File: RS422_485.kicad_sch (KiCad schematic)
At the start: 10 parts, among them U8501 THVD1424

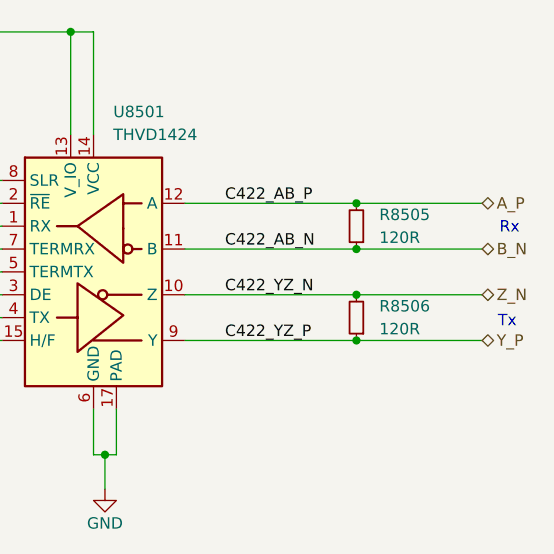
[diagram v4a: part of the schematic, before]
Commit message: added missing heater connectors
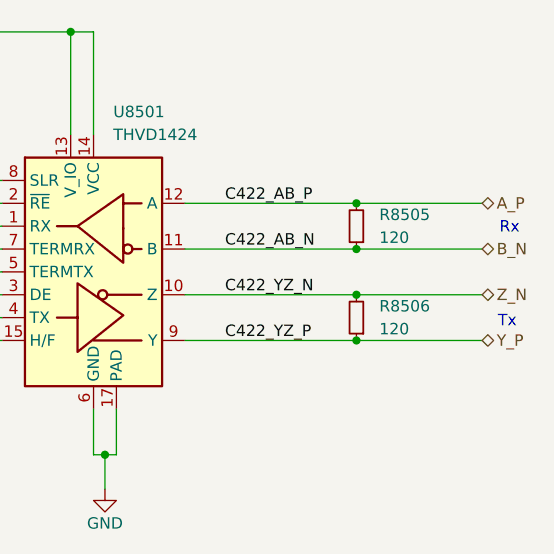
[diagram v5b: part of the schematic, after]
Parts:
- R8505, R8506: value 120R -> 120
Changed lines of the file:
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@@
 			)
 		)
-		(property "Value" "120R"
+		(property "Value" "120"
 			(at 219.71 100.3299 0)
 			(effects
@@
 			)
 		)
-		(property "Value" "120R"
+		(property "Value" "120"
 			(at 219.71 110.4899 0)
 			(effects

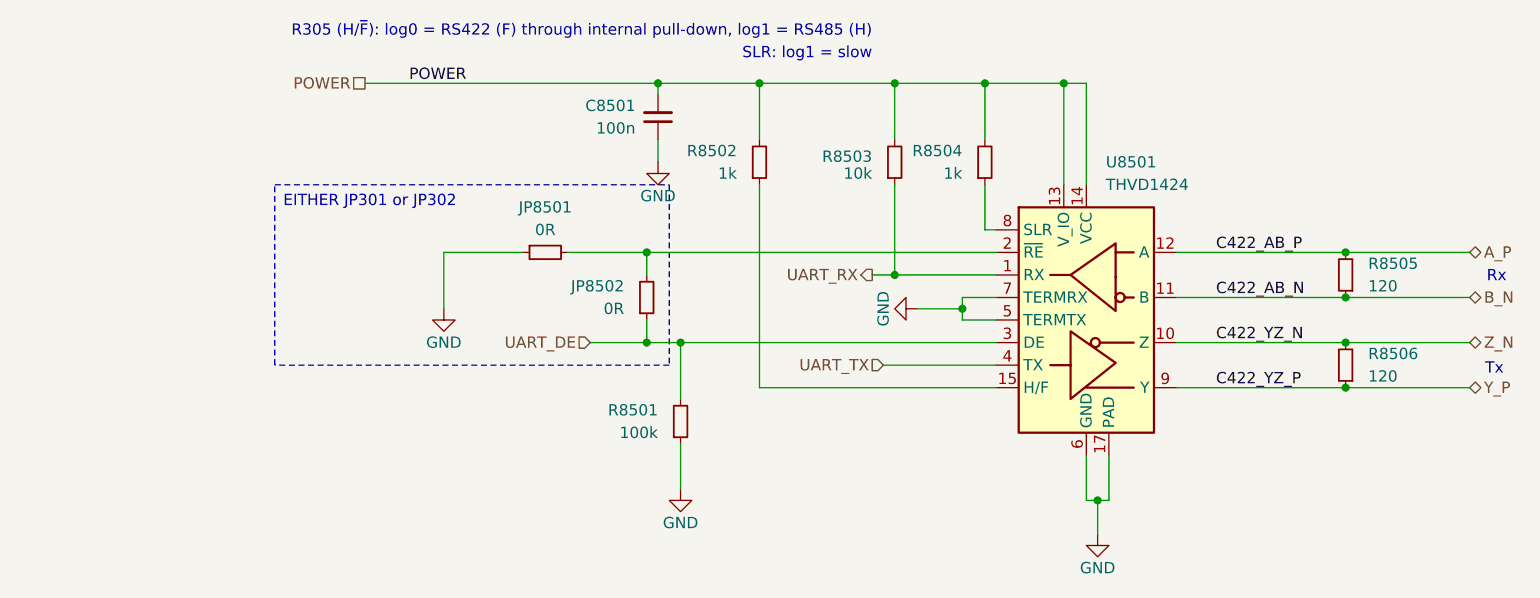
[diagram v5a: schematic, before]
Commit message: restructurization of the entire project improved
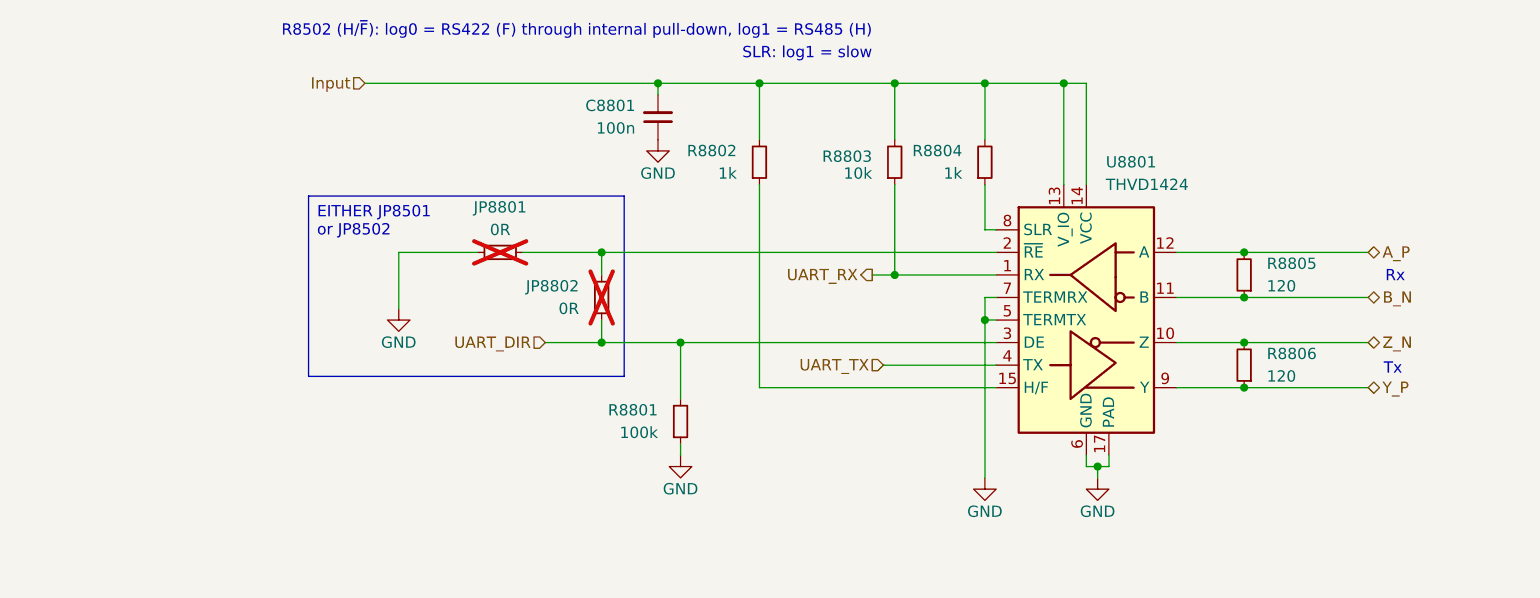
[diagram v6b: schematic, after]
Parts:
- JP8801: renamed from JP8501; now not fitted
- JP8802: renamed from JP8502; now not fitted
- renumbered C8501 to C8801, R8501 to R8801, R8502 to R8802, R8503 to R8803, R8504 to R8804, R8505 to R8805, R8506 to R8806, U8501 to U8801
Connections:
- net POWER renamed Input
- net UART_DE renamed UART_DIR
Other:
- note added: "R8502 (H/~{F}): log0 = RS422 (F) through internal pull-down, log1 = RS485 (H)"
- note removed: "R305 (H/~{F}): log0 = RS422 (F) through internal pull-down, log1 = RS485 (H)"
- moved on the sheet: R8805, R8806

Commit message: added universal switch, added simples current source, reworked test schematic and pcb
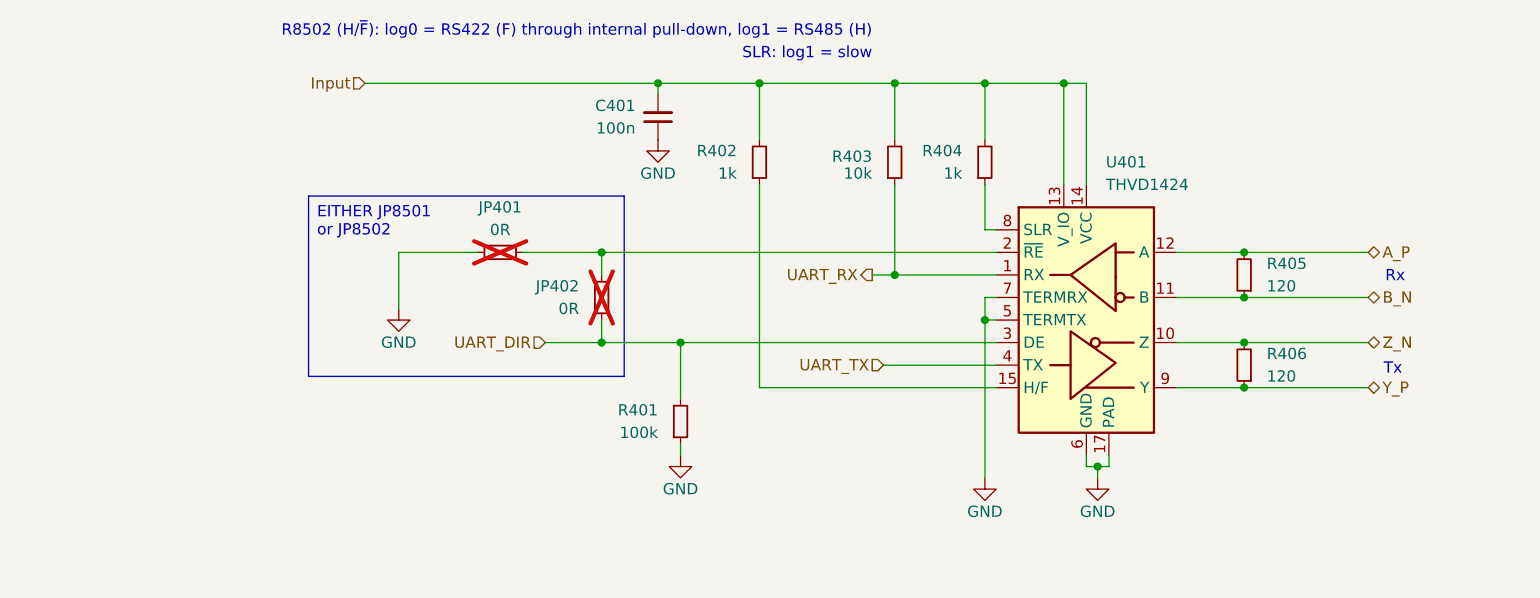
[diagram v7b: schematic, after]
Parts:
- C401: renamed from C8801; footprint Capacitor_SMD:C_0603_1608Metric -> Capacitor_SMD:C_0603_1608Metric_Pad1.08x0.95mm_HandSolder
- renumbered JP8801 to JP401, JP8802 to JP402, R8801 to R401, R8802 to R402, R8803 to R403, R8804 to R404, R8805 to R405, R8806 to R406, U8801 to U401
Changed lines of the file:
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@@
 		(on_board yes)
 		(dnp no)
-		(property "Reference" "R8805"
+		(property "Reference" "R405"
 			(at 208.28 97.7899 0)
 			(effects
@@
 		)
 		(instances
+			(project "EPS_CORE"
+				(path "/29496ace-b476-4f24-a65f-9da1dd70122c/59fca87d-eab6-4325-93c7-8130e49f891e/6fcf384b-60b0-45a5-8dc1-cf23d8e5c23c"
+					(reference "R405")
+					(unit 1)
+				)
+			)
 			(project "EPS_CORE"
 				(path "/43e5e7c8-e7e0-4528-9a3e-b1557849918d/ce55ed75-3d20-4bd3-84d2-d62dbd0d02de/6fcf384b-60b0-45a5-8dc1-cf23d8e5c23c"
@@
 		(on_board yes)
 		(dnp no)
-		(property "Reference" "R8803"
+		(property "Reference" "R403"
 			(at 163.83 85.725 0)
 			(effects
@@
 		)
 		(instances
+			(project "EPS_CORE"
+				(path "/29496ace-b476-4f24-a65f-9da1dd70122c/59fca87d-eab6-4325-93c7-8130e49f891e/6fcf384b-60b0-45a5-8dc1-cf23d8e5c23c"
+					(reference "R403")
+					(unit 1)
+				)
+			)
 			(project "EPS_CORE"
 				(path "/43e5e7c8-e7e0-4528-9a3e-b1557849918d/ce55ed75-3d20-4bd3-84d2-d62dbd0d02de/6fcf384b-60b0-45a5-8dc1-cf23d8e5c23c"
@@
 		(dnp yes)
 		(fields_autoplaced yes)
-		(property "Reference" "JP8801"
+		(property "Reference" "JP401"
 			(at 121.92 91.44 90)
 			(effects
@@
 		)
 		(instances
+			(project "EPS_CORE"
+				(path "/29496ace-b476-4f24-a65f-9da1dd70122c/59fca87d-eab6-4325-93c7-8130e49f891e/6fcf384b-60b0-45a5-8dc1-cf23d8e5c23c"
+					(reference "JP401")
+					(unit 1)
+				)
+			)
 			(project "EPS_CORE"
 				(path "/43e5e7c8-e7e0-4528-9a3e-b1557849918d/ce55ed75-3d20-4bd3-84d2-d62dbd0d02de/6fcf384b-60b0-45a5-8dc1-cf23d8e5c23c"
@@
 		(on_board yes)
 		(dnp no)
-		(property "Reference" "#PWR08803"
+		(property "Reference" "#PWR0403"
 			(at 142.24 125.73 0)
 			(effects
@@
 		)
 		(instances
+			(project "EPS_CORE"
+				(path "/29496ace-b476-4f24-a65f-9da1dd70122c/59fca87d-eab6-4325-93c7-8130e49f891e/6fcf384b-60b0-45a5-8dc1-cf23d8e5c23c"
+					(reference "#PWR0403")
+					(unit 1)
+				)
+			)
 			(project "EPS_CORE"
 				(path "/43e5e7c8-e7e0-4528-9a3e-b1557849918d/ce55ed75-3d20-4bd3-84d2-d62dbd0d02de/6fcf384b-60b0-45a5-8dc1-cf23d8e5c23c"
@@
 		(dnp no)
 		(fields_autoplaced yes)
-		(property "Reference" "C8801"
+		(property "Reference" "C401"
 			(at 137.16 80.0035 0)
 			(effects
@@
 			)
 		)
-		(property "Footprint" "Capacitor_SMD:C_0603_1608Metric"
+		(property "Footprint" "Capacitor_SMD:C_0603_1608Metric_Pad1.08x0.95mm_HandSolder"
 			(at 139.7 81.28 0)
 			(effects
@@
 		)
 		(instances
+			(project "EPS_CORE"
+				(path "/29496ace-b476-4f24-a65f-9da1dd70122c/59fca87d-eab6-4325-93c7-8130e49f891e/6fcf384b-60b0-45a5-8dc1-cf23d8e5c23c"
+					(reference "C401")
+					(unit 1)
+				)
+			)
 			(project "EPS_CORE"
 				(path "/43e5e7c8-e7e0-4528-9a3e-b1557849918d/ce55ed75-3d20-4bd3-84d2-d62dbd0d02de/6fcf384b-60b0-45a5-8dc1-cf23d8e5c23c"
@@
 		(dnp no)
 		(fields_autoplaced yes)
-		(property "Reference" "R8802"
+		(property "Reference" "R402"
 			(at 148.59 85.09 0)
 			(effects
@@
 		)
 		(instances
+			(project "EPS_CORE"
+				(path "/29496ace-b476-4f24-a65f-9da1dd70122c/59fca87d-eab6-4325-93c7-8130e49f891e/6fcf384b-60b0-45a5-8dc1-cf23d8e5c23c"
+					(reference "R402")
+					(unit 1)
+				)
+			)
 			(project "EPS_CORE"
 				(path "/43e5e7c8-e7e0-4528-9a3e-b1557849918d/ce55ed75-3d20-4bd3-84d2-d62dbd0d02de/6fcf384b-60b0-45a5-8dc1-cf23d8e5c23c"
@@
 		(on_board yes)
 		(dnp no)
-		(property "Reference" "#PWR08805"
+		(property "Reference" "#PWR0405"
 			(at 189.23 128.27 0)
 			(effects
@@
 		)
 		(instances
+			(project "EPS_CORE"
+				(path "/29496ace-b476-4f24-a65f-9da1dd70122c/59fca87d-eab6-4325-93c7-8130e49f891e/6fcf384b-60b0-45a5-8dc1-cf23d8e5c23c"
+					(reference "#PWR0405")
+					(unit 1)
+				)
+			)
 			(project "EPS_CORE"
 				(path "/43e5e7c8-e7e0-4528-9a3e-b1557849918d/ce55ed75-3d20-4bd3-84d2-d62dbd0d02de/6fcf384b-60b0-45a5-8dc1-cf23d8e5c23c"
@@
 		(dnp no)
 		(fields_autoplaced yes)
-		(property "Reference" "R8804"
+		(property "Reference" "R404"
 			(at 173.99 85.09 0)
 			(effects
@@
 		)
 		(instances
+			(project "EPS_CORE"
+				(path "/29496ace-b476-4f24-a65f-9da1dd70122c/59fca87d-eab6-4325-93c7-8130e49f891e/6fcf384b-60b0-45a5-8dc1-cf23d8e5c23c"
+					(reference "R404")
+					(unit 1)
+				)
+			)
 			(project "EPS_CORE"
 				(path "/43e5e7c8-e7e0-4528-9a3e-b1557849918d/ce55ed75-3d20-4bd3-84d2-d62dbd0d02de/6fcf384b-60b0-45a5-8dc1-cf23d8e5c23c"
@@
 		(on_board yes)
 		(dnp no)
-		(property "Reference" "#PWR08801"
+		(property "Reference" "#PWR0401"
 			(at 110.49 109.22 0)
 			(effects
@@
 		)
 		(instances
+			(project "EPS_CORE"
+				(path "/29496ace-b476-4f24-a65f-9da1dd70122c/59fca87d-eab6-4325-93c7-8130e49f891e/6fcf384b-60b0-45a5-8dc1-cf23d8e5c23c"
+					(reference "#PWR0401")
+					(unit 1)
+				)
+			)
 			(project "EPS_CORE"
 				(path "/43e5e7c8-e7e0-4528-9a3e-b1557849918d/ce55ed75-3d20-4bd3-84d2-d62dbd0d02de/6fcf384b-60b0-45a5-8dc1-cf23d8e5c23c"
@@
 		(dnp no)
 		(fields_autoplaced yes)
-		(property "Reference" "R8801"
+		(property "Reference" "R401"
 			(at 139.7 114.2999 0)
 			(effects
@@
 		)
 		(instances
+			(project "EPS_CORE"
+				(path "/29496ace-b476-4f24-a65f-9da1dd70122c/59fca87d-eab6-4325-93c7-8130e49f891e/6fcf384b-60b0-45a5-8dc1-cf23d8e5c23c"
+					(reference "R401")
+					(unit 1)
+				)
+			)
 			(project "EPS_CORE"
 				(path "/43e5e7c8-e7e0-4528-9a3e-b1557849918d/ce55ed75-3d20-4bd3-84d2-d62dbd0d02de/6fcf384b-60b0-45a5-8dc1-cf23d8e5c23c"
@@
 		(dnp no)
 		(fields_autoplaced yes)
-		(property "Reference" "U8801"
+		(property "Reference" "U401"
 			(at 190.1541 86.36 0)
 			(effects
@@
 		)
 		(instances
+			(project "EPS_CORE"
+				(path "/29496ace-b476-4f24-a65f-9da1dd70122c/59fca87d-eab6-4325-93c7-8130e49f891e/6fcf384b-60b0-45a5-8dc1-cf23d8e5c23c"
+					(reference "U401")
+					(unit 1)
+				)
+			)
 			(project "EPS_CORE"
 				(path "/43e5e7c8-e7e0-4528-9a3e-b1557849918d/ce55ed75-3d20-4bd3-84d2-d62dbd0d02de/6fcf384b-60b0-45a5-8dc1-cf23d8e5c23c"
@@
 		(on_board yes)
 		(dnp no)
-		(property "Reference" "#PWR08804"
+		(property "Reference" "#PWR0404"
 			(at 176.53 128.27 0)
 			(effects
@@
 		)
 		(instances
+			(project "EPS_CORE"
+				(path "/29496ace-b476-4f24-a65f-9da1dd70122c/59fca87d-eab6-4325-93c7-8130e49f891e/6fcf384b-60b0-45a5-8dc1-cf23d8e5c23c"
+					(reference "#PWR0404")
+					(unit 1)
+				)
+			)
 			(project "EPS_CORE"
 				(path "/43e5e7c8-e7e0-4528-9a3e-b1557849918d/ce55ed75-3d20-4bd3-84d2-d62dbd0d02de/6fcf384b-60b0-45a5-8dc1-cf23d8e5c23c"
@@
 		(on_board yes)
 		(dnp no)
-		(property "Reference" "R8806"
+		(property "Reference" "R406"
 			(at 208.28 107.9499 0)
 			(effects
@@
 		)
 		(instances
+			(project "EPS_CORE"
+				(path "/29496ace-b476-4f24-a65f-9da1dd70122c/59fca87d-eab6-4325-93c7-8130e49f891e/6fcf384b-60b0-45a5-8dc1-cf23d8e5c23c"
+					(reference "R406")
+					(unit 1)
+				)
+			)
 			(project "EPS_CORE"
 				(path "/43e5e7c8-e7e0-4528-9a3e-b1557849918d/ce55ed75-3d20-4bd3-84d2-d62dbd0d02de/6fcf384b-60b0-45a5-8dc1-cf23d8e5c23c"
@@
 		(on_board yes)
 		(dnp no)
-		(property "Reference" "#PWR08802"
+		(property "Reference" "#PWR0402"
 			(at 139.7 90.17 0)
 			(effects
@@
 		)
 		(instances
+			(project "EPS_CORE"
+				(path "/29496ace-b476-4f24-a65f-9da1dd70122c/59fca87d-eab6-4325-93c7-8130e49f891e/6fcf384b-60b0-45a5-8dc1-cf23d8e5c23c"
+					(reference "#PWR0402")
+					(unit 1)
+				)
+			)
 			(project "EPS_CORE"
 				(path "/43e5e7c8-e7e0-4528-9a3e-b1557849918d/ce55ed75-3d20-4bd3-84d2-d62dbd0d02de/6fcf384b-60b0-45a5-8dc1-cf23d8e5c23c"
@@
 		(dnp yes)
 		(fields_autoplaced yes)
-		(property "Reference" "JP8802"
+		(property "Reference" "JP402"
 			(at 130.81 100.33 0)
 			(effects
@@
 		(instances
 			(project "EPS_CORE"
+				(path "/29496ace-b476-4f24-a65f-9da1dd70122c/59fca87d-eab6-4325-93c7-8130e49f891e/6fcf384b-60b0-45a5-8dc1-cf23d8e5c23c"
+					(reference "JP402")
+					(unit 1)
+				)
+			)
+			(project "EPS_CORE"
 				(path "/43e5e7c8-e7e0-4528-9a3e-b1557849918d/ce55ed75-3d20-4bd3-84d2-d62dbd0d02de/6fcf384b-60b0-45a5-8dc1-cf23d8e5c23c"

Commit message: Minor changes to acomodate jlcpcb guidelines, this version ordered
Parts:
- JP401, JP402, R401, R402, R403, R404, R405, R406: footprint Resistor_SMD:R_0603_1608Metric -> Resistor_SMD:R_0603_1608Metric_Pad0.98x0.95mm_HandSolder
